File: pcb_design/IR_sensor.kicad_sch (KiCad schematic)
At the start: 32 parts, among them J6 IR_1, J7 IR_3, J8 IR_2, J9 IR_4, Q2 DMN3065LW-7, Q3 DMN3065LW-7, Q4 DMN3065LW-7, Q5 DMN3065LW-7

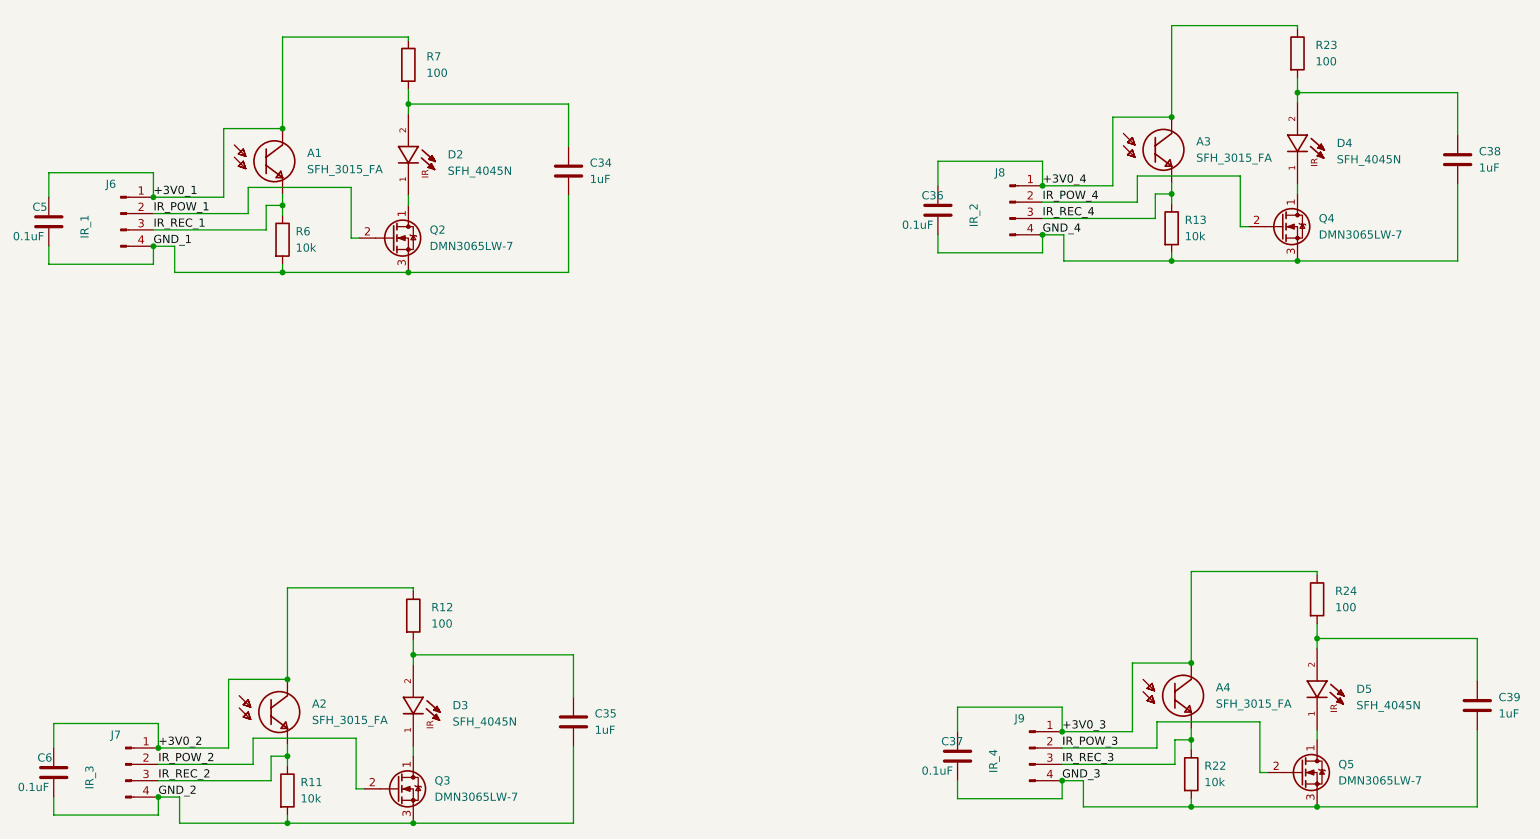
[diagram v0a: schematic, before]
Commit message: Add resistors between MOSFET gate
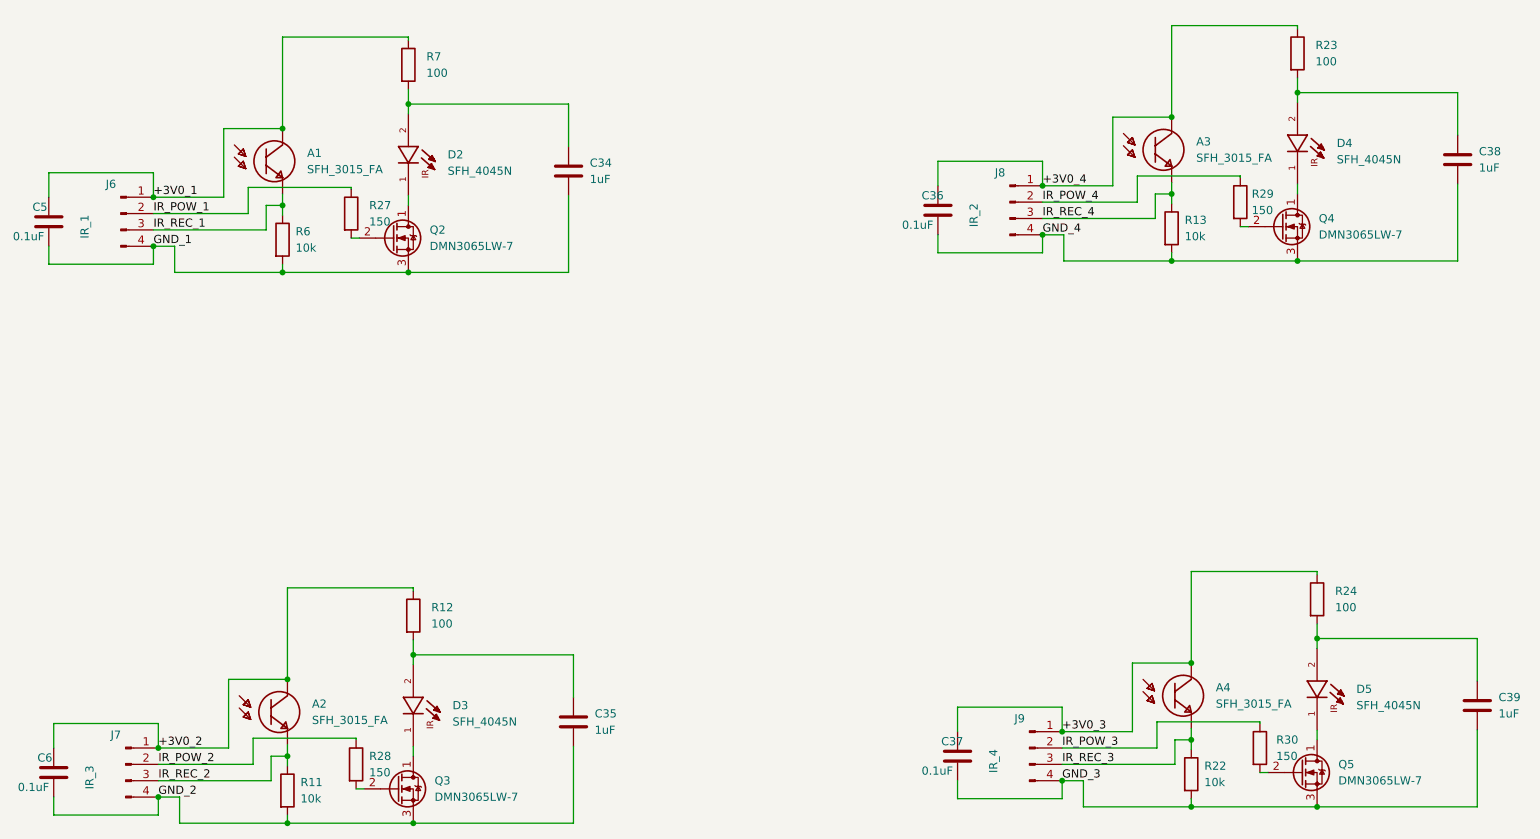
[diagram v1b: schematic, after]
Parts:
- added R27, R28, R29, R30: 150, Resistor_SMD:R_0402_1005Metric, symbol Device:R
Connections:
- net IR_POW_1: now also R27.1; no longer Q2.2 (G)
- net IR_POW_2: now also R28.1; no longer Q3.2 (G)
- net IR_POW_3: now also R30.1; no longer Q5.2 (G)
- net IR_POW_4: now also R29.1; no longer Q4.2 (G)
- new net: Q5.2 (G), R30.2
- new net: Q2.2 (G), R27.2
- new net: Q4.2 (G), R29.2
- new net: Q3.2 (G), R28.2
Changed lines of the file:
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@@
     (stroke (width 0) (type default) (color 0 0 0 0))
   )
-  (wire (pts (xy 75.438 146.558) (xy 75.438 154.432))
+  (wire (pts (xy 75.438 146.558) (xy 75.438 146.812))
     (stroke (width 0) (type default) (color 0 0 0 0))
   )
@@
     (stroke (width 0) (type default) (color 0 0 0 0))
   )
-  (wire (pts (xy 215.9 144.018) (xy 215.9 151.892))
+  (wire (pts (xy 215.9 144.018) (xy 215.9 144.272))
     (stroke (width 0) (type default) (color 0 0 0 0))
   )
@@
     (stroke (width 0) (type default) (color 0 0 0 0))
   )
-  (wire (pts (xy 74.676 60.96) (xy 74.676 68.834))
+  (wire (pts (xy 74.676 60.96) (xy 74.676 61.214))
     (stroke (width 0) (type default) (color 0 0 0 0))
   )
@@
     (stroke (width 0) (type default) (color 0 0 0 0))
   )
-  (wire (pts (xy 212.852 59.182) (xy 212.852 67.056))
+  (wire (pts (xy 212.852 59.182) (xy 212.852 59.436))
     (stroke (width 0) (type default) (color 0 0 0 0))
   )
@@
     (pin "2")
   )
+  (symbol (lib_id "Device:R") (at 215.9 148.082 0) (unit 1)
+    (in_bom yes) (on_board yes) (fields_autoplaced)
+    (property "Reference" "R30" (id 0) (at 218.44 146.8119 0)
+      (effects (font (size 1.27 1.27)) (justify left))
+    )
+    (property "Value" "150" (id 1) (at 218.44 149.3519 0)
+      (effects (font (size 1.27 1.27)) (justify left))
+    )
+    (property "Footprint" "Resistor_SMD:R_0402_1005Metric" (id 2) (at 214.122 148.082 90)
+      (effects (font (size 1.27 1.27)) hide)
+    )
+    (property "Datasheet" "~" (id 3) (at 215.9 148.082 0)
+      (effects (font (size 1.27 1.27)) hide)
+    )
+    (pin "1")
+    (pin "2")
+  )
   (symbol (lib_id "Device:R") (at 64.77 154.686 0) (unit 1)
     (in_bom yes) (on_board yes) (fields_autoplaced)
@@
     (property "STANDARD" "Manufacturer Recommendations" (id 7) (at 84.328 142.748 0)
       (effects (font (size 1.27 1.27)) (justify left bottom) hide)
+    )
+    (pin "1")
+    (pin "2")
+  )
+  (symbol (lib_id "Device:R") (at 74.676 65.024 0) (unit 1)
+    (in_bom yes) (on_board yes) (fields_autoplaced)
+    (property "Reference" "R27" (id 0) (at 77.47 63.7539 0)
+      (effects (font (size 1.27 1.27)) (justify left))
+    )
+    (property "Value" "150" (id 1) (at 77.47 66.2939 0)
+      (effects (font (size 1.27 1.27)) (justify left))
+    )
+    (property "Footprint" "Resistor_SMD:R_0402_1005Metric" (id 2) (at 72.898 65.024 90)
+      (effects (font (size 1.27 1.27)) hide)
+    )
+    (property "Datasheet" "~" (id 3) (at 74.676 65.024 0)
+      (effects (font (size 1.27 1.27)) hide)
     )
     (pin "1")
@@
     (pin "3")
   )
+  (symbol (lib_id "Device:R") (at 212.852 63.246 0) (unit 1)
+    (in_bom yes) (on_board yes) (fields_autoplaced)
+    (property "Reference" "R29" (id 0) (at 214.63 61.9759 0)
+      (effects (font (size 1.27 1.27)) (justify left))
+    )
+    (property "Value" "150" (id 1) (at 214.63 64.5159 0)
+      (effects (font (size 1.27 1.27)) (justify left))
+    )
+    (property "Footprint" "Resistor_SMD:R_0402_1005Metric" (id 2) (at 211.074 63.246 90)
+      (effects (font (size 1.27 1.27)) hide)
+    )
+    (property "Datasheet" "~" (id 3) (at 212.852 63.246 0)
+      (effects (font (size 1.27 1.27)) hide)
+    )
+    (pin "1")
+    (pin "2")
+  )
   (symbol (lib_id "Device:R") (at 202.184 67.31 0) (unit 1)
     (in_bom yes) (on_board yes) (fields_autoplaced)
@@
     )
     (pin "1")
+    (pin "2")
+  )
+  (symbol (lib_id "Device:R") (at 75.438 150.622 0) (unit 1)
+    (in_bom yes) (on_board yes) (fields_autoplaced)
+    (property "Reference" "R28" (id 0) (at 77.47 149.3519 0)
+      (effects (font (size 1.27 1.27)) (justify left))
+    )
+    (property "Value" "150" (id 1) (at 77.47 151.8919 0)
+      (effects (font (size 1.27 1.27)) (justify left))
+    )
+    (property "Footprint" "Resistor_SMD:R_0402_1005Metric" (id 2) (at 73.66 150.622 90)
+      (effects (font (size 1.27 1.27)) hide)
+    )
+    (property "Datasheet" "~" (id 3) (at 75.438 150.622 0)
+      (effects (font (size 1.27 1.27)) hide)
+    )
+    (pin "1")

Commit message: Update Mushak PCB design to include new features (#5)
* Update mushak PCB with new changes
* Add AMS1117 as 3.3v regulator
* Add new alternate placement for IR sensors
* Add new 3.3v compatible ToF sensor
* Update gerber files

* Add changes to silkscreen and filter capacitors
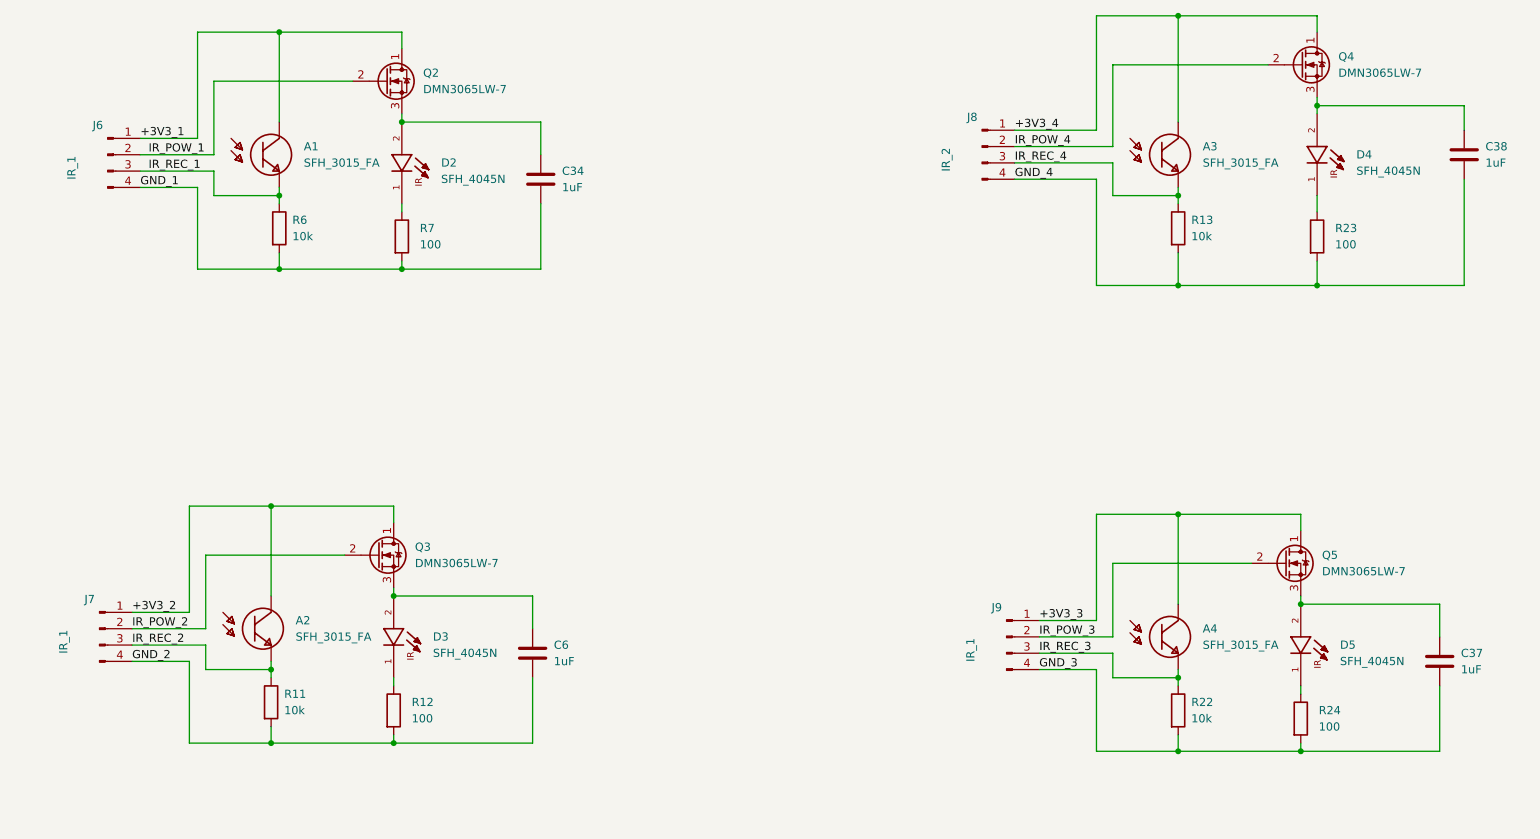
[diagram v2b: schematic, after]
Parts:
- removed C35, C39: 1uF, Capacitor_SMD:C_0603_1608Metric, symbol Device:C
- removed C36, C5: 0.1uF, Capacitor_SMD:C_0402_1005Metric, symbol Device:C
- removed R27, R28, R29, R30: 150, Resistor_SMD:R_0402_1005Metric, symbol Device:R
- C37, C6: value 0.1uF -> 1uF; footprint Capacitor_SMD:C_0402_1005Metric -> Capacitor_SMD:C_0603_1608Metric
- J7: value IR_3 -> IR_1
- J9: value IR_4 -> IR_1
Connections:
- net GND_1: now also R7.2; no longer Q2.3 (S)
- net GND_2: now also R12.2; no longer Q3.3 (S)
- net GND_3: now also R24.2; no longer Q5.3 (S)
- net GND_4: now also R23.2; no longer Q4.3 (S)
- net IR_POW_1: now also Q2.2 (G)
- net IR_POW_2: now also Q3.2 (G)
- net IR_POW_3: now also Q5.2 (G)
- net IR_POW_4: now also Q4.2 (G)
- net at D4.1: now also R23.1; no longer Q4.1 (D)
- net at C38.1, D4.2: now also Q4.3 (S); no longer R23.2
- net at D3.1: now also R12.1; no longer Q3.1 (D)
- net at D3.2: now also C6.1, Q3.3 (S); no longer R12.2
- net at C34.1, D2.2: now also Q2.3 (S); no longer R7.2
- net at D2.1: now also R7.1; no longer Q2.1 (D)
- net at D5.1: now also R24.1; no longer Q5.1 (D)
- net at D5.2: now also C37.1, Q5.3 (S); no longer R24.2
- net +3V0_1 renamed +3V3_1
- net +3V3_1: now also Q2.1 (D); no longer R7.1
- net +3V0_2 renamed +3V3_2
- net +3V3_2: now also Q3.1 (D); no longer C6.1, R12.1
- net +3V0_3 renamed +3V3_3
- net +3V3_3: now also Q5.1 (D); no longer C37.1, R24.1
- net +3V0_4 renamed +3V3_4
- net +3V3_4: now also Q4.1 (D); no longer R23.1
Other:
- moved on the sheet: A1, A3, C34, C38, D2, D4, J6, J8, Q2, Q4, R13, R23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
